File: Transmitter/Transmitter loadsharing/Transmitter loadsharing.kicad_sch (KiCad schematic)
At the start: 111 parts, among them J1 Conn_Coaxial, J10 Conn_01x01, J11 Conn_01x01, J12 Conn_01x01, J13 Conn_01x01, J14 Conn_01x01, J15 Conn_01x01, J16 Conn_01x01, J17 Conn_Coaxial, J18 Conn_Coaxial, J19 Conn_Coaxial, J2 Conn_01x03, J20 Conn_01x01, J21 Conn_01x01, J22 Conn_01x01, J23 Conn_01x01, J3 Conn_01x03, J4 Conn_01x02_Socket, J5 Conn_01x02, J6 Conn_01x01, J7 Conn_01x02, J8 Conn_01x02_Socket, J9 Conn_01x01, U1 OPA3692IDBQR, U10 LT3094EMSE-PBF, U11 LT3094EMSE-PBF, U2 THS3091D, U3 THS3091D, U4 THS3091D, U5 THS3091D, U6 THS3091D, U7 THS3091D, U8 LT3045EMSE-PBF, U9 LT3045EMSE-PBF

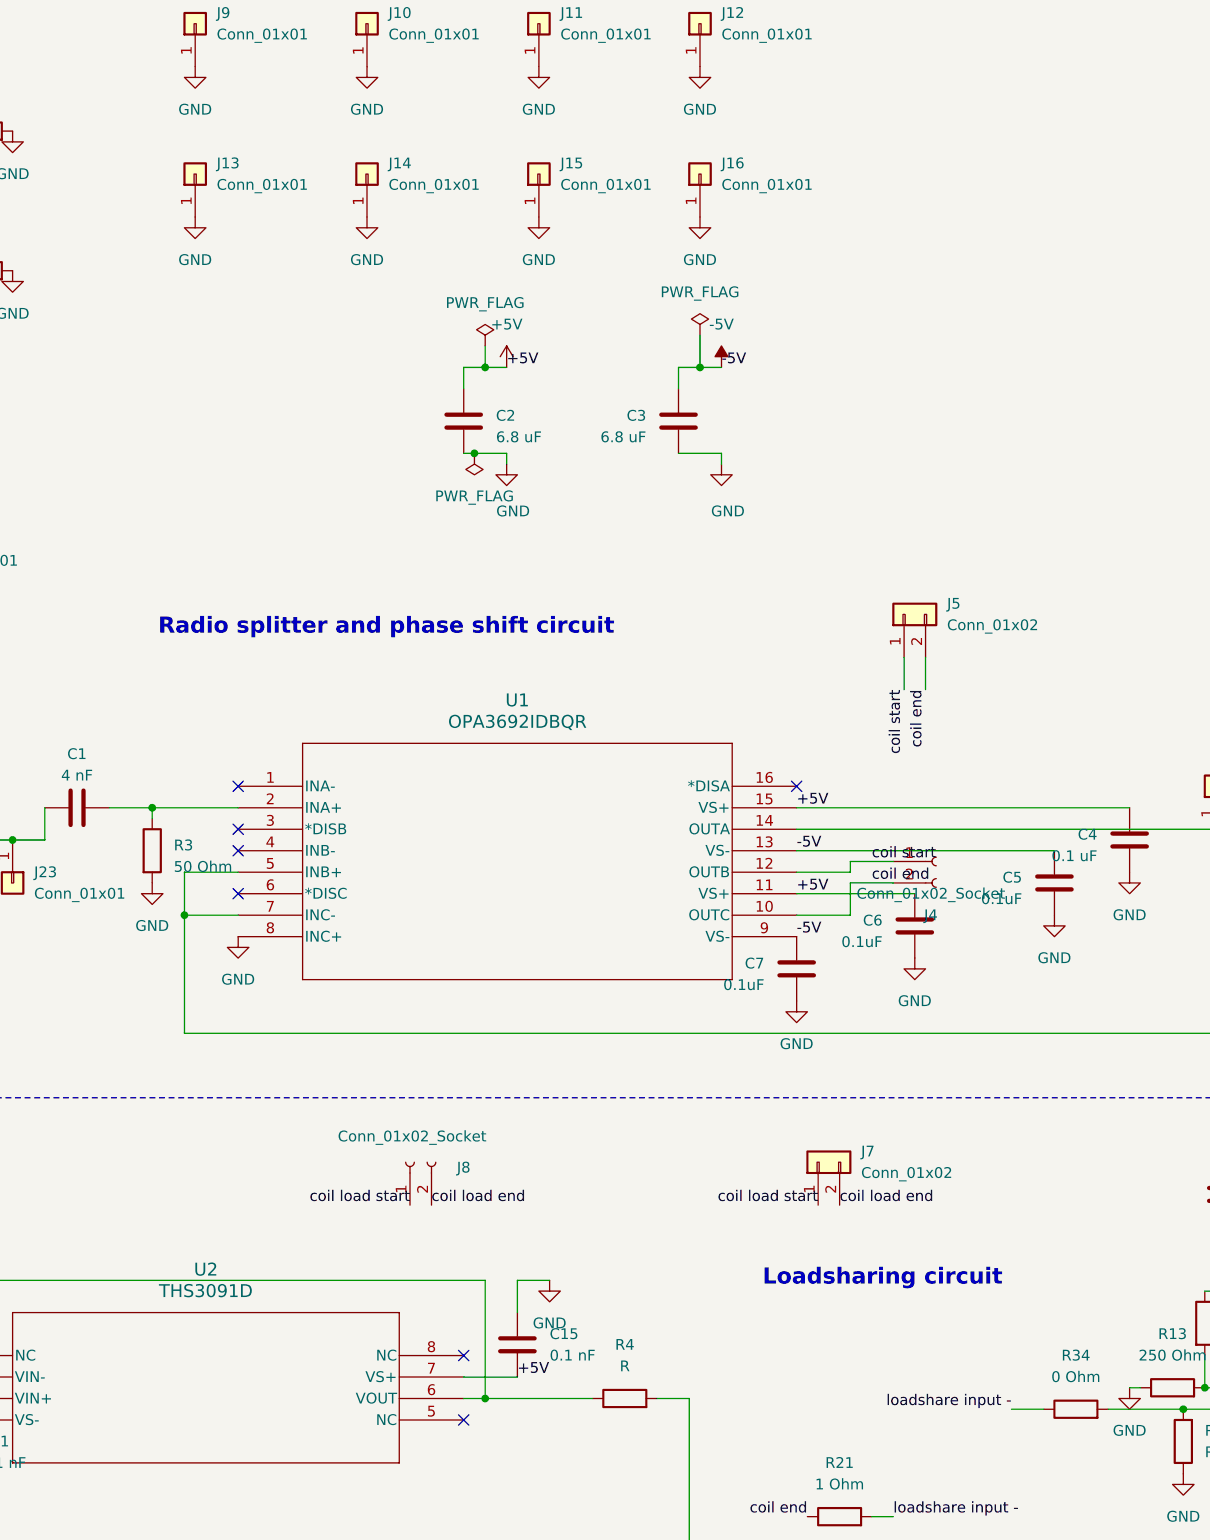
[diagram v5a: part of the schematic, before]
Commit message: Added test point after HPF and§ capactitors for coil tuning
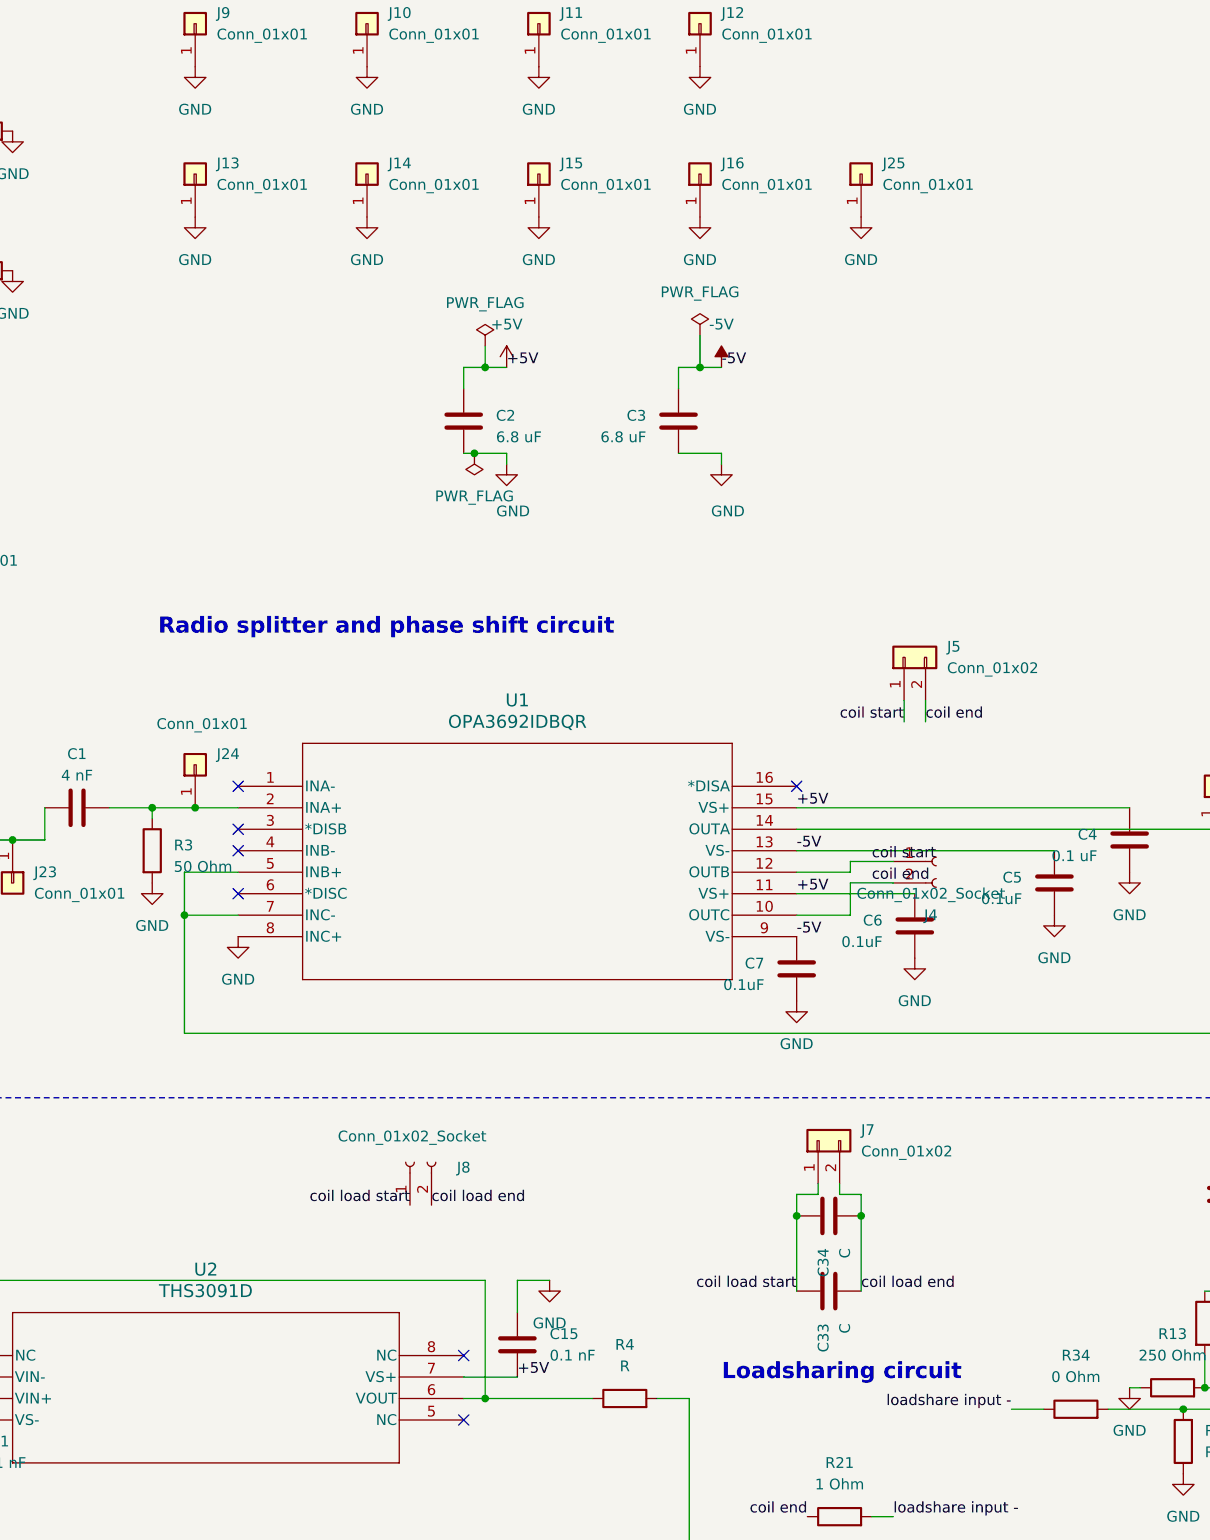
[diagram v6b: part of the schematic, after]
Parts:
- added C33, C34: C, Capacitor_SMD:C_0603_1608Metric_Pad1.08x0.95mm_HandSolder, symbol Device:C
- added J24, J25: Conn_01x01, Connector_PinHeader_2.54mm:PinHeader_1x01_P2.54mm_Vertical, symbol Connector_Generic:Conn_01x01
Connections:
- net GND: now also J25.1 (Pin_1)
- net coil load end: now also C33.1, C34.1
- net coil load start: now also C33.2, C34.2
- net at C1.2, R3.1, U1.2 (INA+): now also J24.1 (Pin_1)
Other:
- moved on the sheet: J5, J7

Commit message: version before review with Saul
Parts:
- C11, C12, C13, C15, C16, C17, C19, C20, C21, C23, C24, C25: value 0.1 nF -> 0.1 uF
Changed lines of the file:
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@@
 			)
 		)
-		(property "Value" "0.1 nF"
+		(property "Value" "0.1 uF"
 			(at 280.67 175.2599 0)
 			(effects
@@
 			)
 		)
-		(property "Value" "0.1 nF"
+		(property "Value" "0.1 uF"
 			(at 212.09 253.9999 0)
 			(effects
@@
 			)
 		)
-		(property "Value" "0.1 nF"
+		(property "Value" "0.1 uF"
 			(at 59.69 219.7099 0)
 			(effects
@@
 			)
 		)
-		(property "Value" "0.1 nF"
+		(property "Value" "0.1 uF"
 			(at 58.42 252.7299 0)
 			(effects
@@
 			)
 		)
-		(property "Value" "0.1 nF"
+		(property "Value" "0.1 uF"
 			(at 59.69 186.6899 0)
 			(effects
@@
 			)
 		)
-		(property "Value" "0.1 nF"
+		(property "Value" "0.1 uF"
 			(at 127 173.9899 0)
 			(effects
@@
 			)
 		)
-		(property "Value" "0.1 nF"
+		(property "Value" "0.1 uF"
 			(at 213.36 187.9599 0)
 			(effects
@@
 			)
 		)
-		(property "Value" "0.1 nF"
+		(property "Value" "0.1 uF"
 			(at 127 207.0099 0)
 			(effects
@@
 			)
 		)
-		(property "Value" "0.1 nF"
+		(property "Value" "0.1 uF"
 			(at 280.67 208.2799 0)
 			(effects
@@
 			)
 		)
-		(property "Value" "0.1 nF"
+		(property "Value" "0.1 uF"
 			(at 213.36 220.9799 0)
 			(effects
@@
 			)
 		)
-		(property "Value" "0.1 nF"
+		(property "Value" "0.1 uF"
 			(at 125.73 240.0299 0)
 			(effects
@@
 			)
 		)
-		(property "Value" "0.1 nF"
+		(property "Value" "0.1 uF"
 			(at 279.4 241.2999 0)
 			(effects

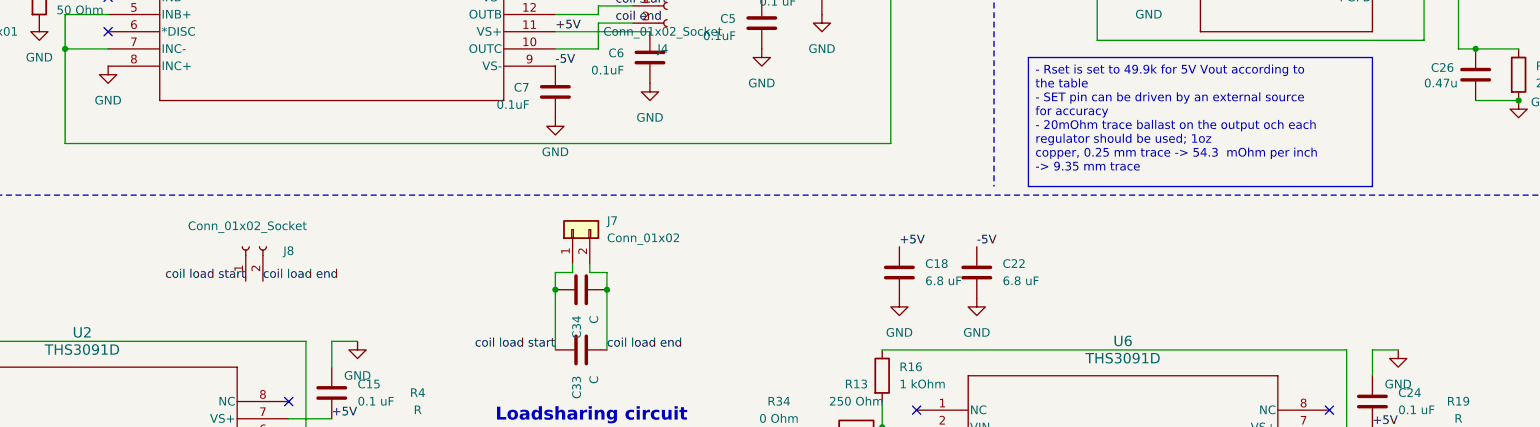
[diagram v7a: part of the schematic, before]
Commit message: Added via stiching to TX board, moved almost all vias off of pads, increased the trace width for the power supply and changed coil connector to horizontal socket
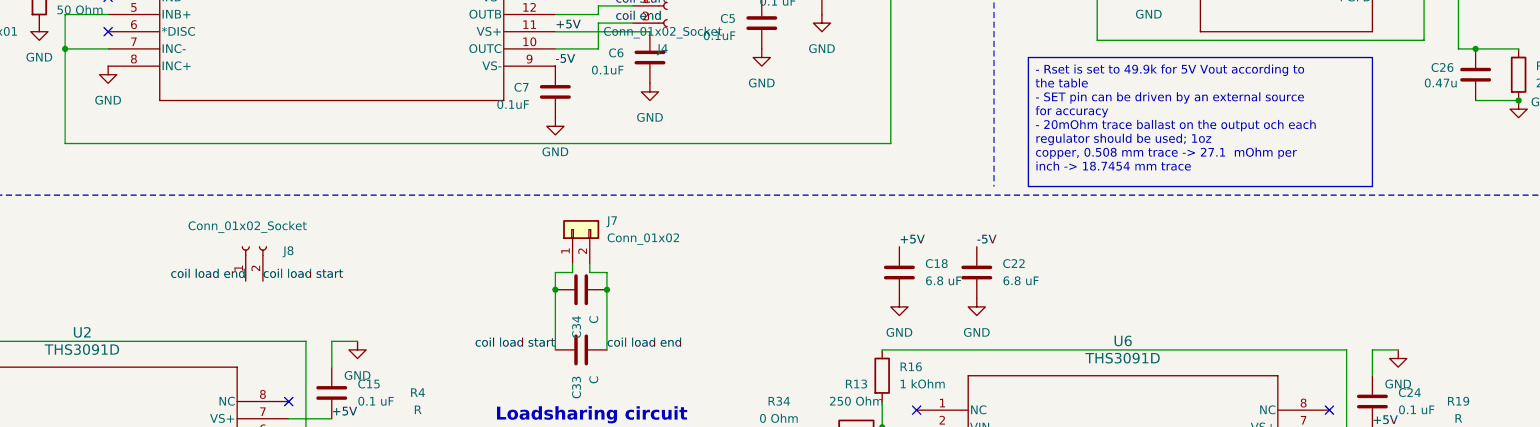
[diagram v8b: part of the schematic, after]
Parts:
- J8: footprint Connector_PinSocket_2.54mm:PinSocket_1x02_P2.54mm_Vertical -> Connector_PinSocket_2.54mm:PinSocket_1x02_P2.54mm_Horizontal
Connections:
- net coil load end: now also J8.1 (Pin_1); no longer J8.2 (Pin_2)
- net coil load start: now also J8.2 (Pin_2); no longer J8.1 (Pin_1)
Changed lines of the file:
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@@
 		)
 	)
-	(text_box "- Rset is set to 49.9k for 5V Vout according to the table  \n- SET pin can be driven by an external source for accuracy\n- 20mOhm trace ballast on the output och each regulator should be used; 1oz\ncopper, 0.25 mm trace -> 54.3  mOhm per inch -> 9.35 mm trace\n"
+	(text_box "- Rset is set to 49.9k for 5V Vout according to the table  \n- SET pin can be driven by an external source for accuracy\n- 20mOhm trace ballast on the output och each regulator should be used; 1oz\ncopper, 0.508 mm trace -> 27.1  mOhm per inch -> 18.7454 mm trace\n"
 		(exclude_from_sim no)
 		(at 226.06 123.19 0)
@@
 		)
 	)
-	(label "coil load end"
-		(at 113.03 156.21 0)
-		(fields_autoplaced yes)
-		(effects
-			(font
-				(size 1.27 1.27)
-			)
-			(justify left bottom)
-		)
-	)
 	(label "-5V"
 		(at 147.32 57.15 0)
@@
 		)
 	)
-	(label "coil load start"
-		(at 110.49 156.21 180)
-		(fields_autoplaced yes)
-		(effects
-			(font
-				(size 1.27 1.27)
-			)
-			(justify right bottom)
-		)
-	)
 	(label "loadshare input +"
 		(at 31.75 179.07 180)
@@
 		)
 	)
+	(label "coil load start"
+		(at 113.03 156.21 0)
+		(fields_autoplaced yes)
+		(effects
+			(font
+				(size 1.27 1.27)
+			)
+			(justify left bottom)
+		)
+	)
 	(label "-5V"
 		(at 45.72 147.32 0)
@@
 			)
 			(justify left bottom)
+		)
+	)
+	(label "coil load end"
+		(at 110.49 156.21 180)
+		(fields_autoplaced yes)
+		(effects
+			(font
+				(size 1.27 1.27)
+			)
+			(justify right bottom)
 		)
 	)
@@
 			)
 		)
-		(property "Footprint" "Connector_PinSocket_2.54mm:PinSocket_1x02_P2.54mm_Vertical"
+		(property "Footprint" "Connector_PinSocket_2.54mm:PinSocket_1x02_P2.54mm_Horizontal"
 			(at 110.49 151.13 0)
 			(effects
